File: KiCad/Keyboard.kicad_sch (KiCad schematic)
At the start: 89 parts, among them J1 USB_C_Receptacle, J2 Conn_01x02_Pin, SW1 SW_RESET, SW10 SW_Z, SW11 SW_SUPER, SW12 SW_2, SW13 SW_W, SW14 SW_S, SW15 SW_X, SW16 SW_ALT, SW17 SW_3, SW18 SW_E, SW19 SW_D, SW2 SW_TICK, SW20 SW_C, SW21 SW_SPACE, SW22 SW_4, SW23 SW_R, SW24 SW_F, SW25 SW_V, SW26 SW_5, SW27 SW_T, SW28 SW_G, SW29 SW_6, SW3 SW_TAB, SW4 SW_CAPS, SW5 SW_SHIFT, SW6 SW_CTRL, SW7 SW_1, SW8 SW_Q, SW9 SW_A, U1 ESP32-C6-MINI-1, U2 USBLC6-2SC6, U4 TPS63031DSK, U5 BQ25185DLHR

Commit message: Assign all footprints
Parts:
- C1, C10, C11, C12, C2, C3, C5, C6, C7, C8, C9: footprint (none) -> Capacitor_SMD:C_0603_1608Metric
- D31, D5: footprint (none) -> LED_SMD:LED_0805_2012Metric
- J1: footprint (none) -> Connector_USB:USB_C_Receptacle_JAE_DX07S016JA1R1500
- J2: footprint (none) -> Connector_JST:JST_PH_S2B-PH-SM4-TB_1x02-1MP_P2.00mm_Horizontal
- L1: footprint (none) -> Inductor_SMD:L_Coilcraft_LPS3010
- R1, R10, R2, R3, R4, R5, R6, R7, R8, R9: footprint (none) -> Resistor_SMD:R_0603_1608Metric
- SW1: footprint (none) -> Button_Switch_SMD:SW_SPDT_CK_JS102011SAQN
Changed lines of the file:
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@@
 			)
 		)
-		(property "Footprint" ""
+		(property "Footprint" "Capacitor_SMD:C_0603_1608Metric"
 			(at 243.84 96.52 0)
 			(hide yes)
@@
 			)
 		)
-		(property "Footprint" ""
+		(property "Footprint" "LED_SMD:LED_0805_2012Metric"
 			(at 279.4 77.47 0)
 			(hide yes)
@@
 			)
 		)
-		(property "Footprint" ""
+		(property "Footprint" "LED_SMD:LED_0805_2012Metric"
 			(at 218.44 115.57 0)
 			(hide yes)
@@
 			)
 		)
-		(property "Footprint" ""
+		(property "Footprint" "Resistor_SMD:R_0603_1608Metric"
 			(at 71.12 167.64 0)
 			(hide yes)
@@
 			)
 		)
-		(property "Footprint" ""
+		(property "Footprint" "Resistor_SMD:R_0603_1608Metric"
 			(at 194.31 48.26 0)
 			(hide yes)
@@
 			)
 		)
-		(property "Footprint" ""
+		(property "Footprint" "Capacitor_SMD:C_0603_1608Metric"
 			(at 278.13 127 0)
 			(hide yes)
@@
 			)
 		)
-		(property "Footprint" ""
+		(property "Footprint" "Inductor_SMD:L_Coilcraft_LPS3010"
 			(at 241.3 120.65 0)
 			(hide yes)
@@
 			)
 		)
-		(property "Footprint" ""
+		(property "Footprint" "Resistor_SMD:R_0603_1608Metric"
 			(at 139.7 139.7 0)
 			(hide yes)
@@
 			)
 		)
-		(property "Footprint" ""
+		(property "Footprint" "Resistor_SMD:R_0603_1608Metric"
 			(at 133.35 163.83 0)
 			(hide yes)
@@
 			)
 		)
-		(property "Footprint" ""
+		(property "Footprint" "Resistor_SMD:R_0603_1608Metric"
 			(at 149.86 146.05 0)
 			(hide yes)
@@
 			)
 		)
-		(property "Footprint" ""
+		(property "Footprint" "Capacitor_SMD:C_0603_1608Metric"
 			(at 82.55 132.08 0)
 			(hide yes)
@@
 			)
 		)
-		(property "Footprint" ""
+		(property "Footprint" "Connector_JST:JST_PH_S2B-PH-SM4-TB_1x02-1MP_P2.00mm_Horizontal"
 			(at 156.21 184.15 0)
 			(hide yes)
@@
 			)
 		)
-		(property "Footprint" ""
+		(property "Footprint" "Capacitor_SMD:C_0603_1608Metric"
 			(at 269.24 127 0)
 			(hide yes)
@@
 			)
 		)
-		(property "Footprint" ""
+		(property "Footprint" "Button_Switch_SMD:SW_SPDT_CK_JS102011SAQN"
 			(at 44.45 134.62 0)
 			(hide yes)
@@
 			)
 		)
-		(property "Footprint" ""
+		(property "Footprint" "Capacitor_SMD:C_0603_1608Metric"
 			(at 44.45 146.05 0)
 			(hide yes)
@@
 			)
 		)
-		(property "Footprint" ""
+		(property "Footprint" "Capacitor_SMD:C_0603_1608Metric"
 			(at 167.64 161.29 0)
 			(hide yes)
@@
 			)
 		)
-		(property "Footprint" ""
+		(property "Footprint" "Resistor_SMD:R_0603_1608Metric"
 			(at 267.97 45.72 0)
 			(hide yes)
@@
 			)
 		)
-		(property "Footprint" ""
+		(property "Footprint" "Connector_USB:USB_C_Receptacle_JAE_DX07S016JA1R1500"
 			(at 247.65 29.21 0)
 			(hide yes)
@@
 			)
 		)
-		(property "Footprint" ""
+		(property "Footprint" "Capacitor_SMD:C_0603_1608Metric"
 			(at 157.48 119.38 0)
 			(hide yes)
@@
 			)
 		)
-		(property "Footprint" ""
+		(property "Footprint" "Capacitor_SMD:C_0603_1608Metric"
 			(at 229.87 144.78 0)
 			(hide yes)
@@
 			)
 		)
-		(property "Footprint" ""
+		(property "Footprint" "Resistor_SMD:R_0603_1608Metric"
 			(at 63.5 134.62 0)
 			(hide yes)
@@
 			)
 		)
-		(property "Footprint" ""
+		(property "Footprint" "Resistor_SMD:R_0603_1608Metric"
 			(at 279.4 86.36 0)
 			(hide yes)
@@
 			)
 		)
-		(property "Footprint" ""
+		(property "Footprint" "Capacitor_SMD:C_0603_1608Metric"
 			(at 63.5 146.05 0)
 			(hide yes)
@@
 			)
 		)
-		(property "Footprint" ""
+		(property "Footprint" "Capacitor_SMD:C_0603_1608Metric"
 			(at 146.05 175.26 0)
 			(hide yes)
@@
 			)
 		)
-		(property "Footprint" ""
+		(property "Footprint" "Capacitor_SMD:C_0603_1608Metric"
 			(at 96.52 132.08 0)
 			(hide yes)
@@
 			)
 		)
-		(property "Footprint" ""
+		(property "Footprint" "Resistor_SMD:R_0603_1608Metric"
 			(at 265.43 55.88 0)
 			(hide yes)
@@
 			)
 		)
-		(property "Footprint" ""
+		(property "Footprint" "Resistor_SMD:R_0603_1608Metric"
 			(at 218.44 104.14 0)
 			(hide yes)

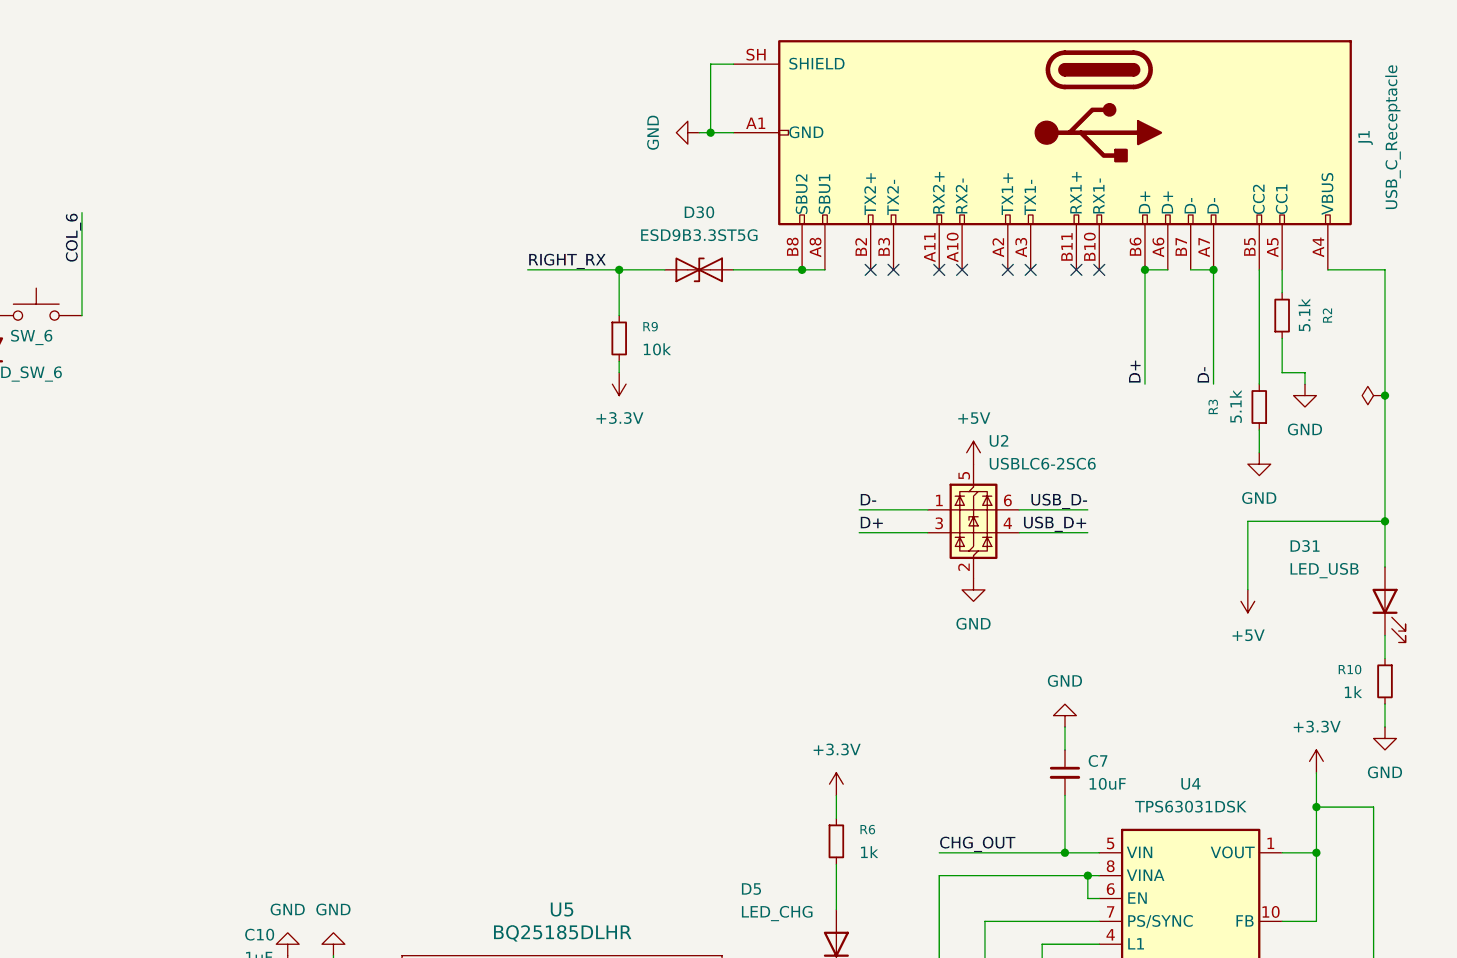
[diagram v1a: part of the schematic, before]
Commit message: Switch to 16-pin USBC
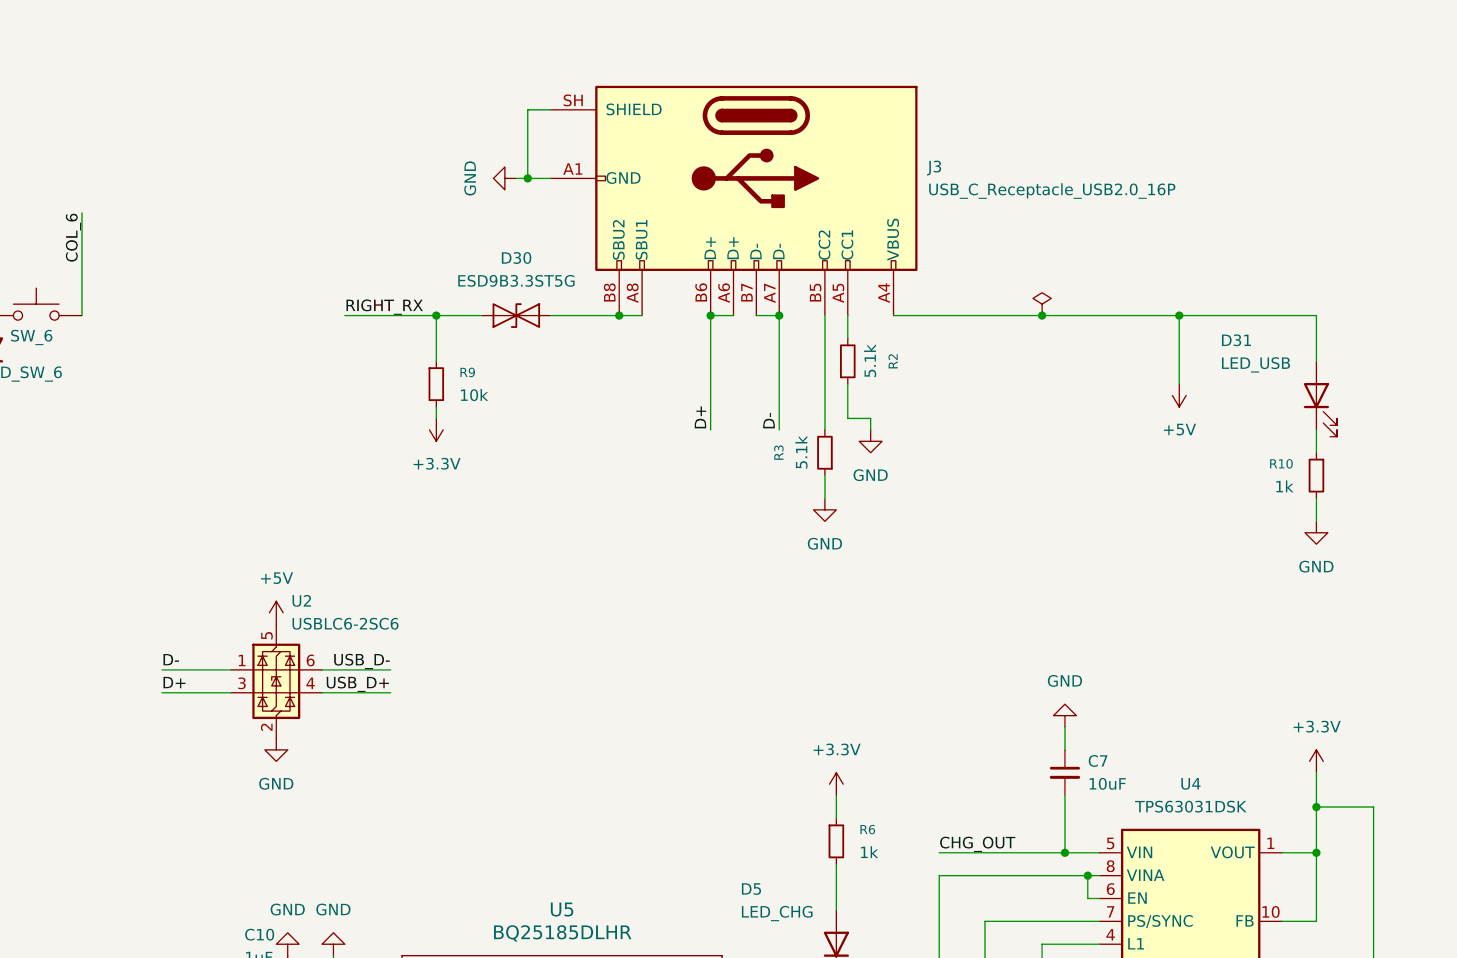
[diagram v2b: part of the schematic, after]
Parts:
- removed J1: USB_C_Receptacle, Connector_USB:USB_C_Receptacle_JAE_DX07S016JA1R1500, symbol Connector:USB_C_Receptacle
- added J3: USB_C_Receptacle_USB2.0_16P, Connector_USB:USB_C_Receptacle_JAE_DX07S016JA1R1500, symbol Connector:USB_C_Receptacle_USB2.0_16P
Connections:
- net +5V: now also J3.A4 (VBUS), J3.A9 (VBUS), J3.B4 (VBUS), J3.B9 (VBUS)
- net D+: now also J3.A6 (D+), J3.B6 (D+)
- net D-: now also J3.A7 (D-), J3.B7 (D-)
- net GND: now also J3.A1 (GND), J3.A12 (GND), J3.B1 (GND), J3.B12 (GND), J3.SH (SHIELD)
- net at D30.2 (A2): now also J3.A8 (SBU1), J3.B8 (SBU2)
- net at R2.2: now also J3.A5 (CC1)
- net at R3.2: now also J3.B5 (CC2)
- no-connect marks 12 -> 4
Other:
- moved on the sheet: D30, D31, R10, R2, R3, R9, U2

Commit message: Start PCB layout
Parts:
- C10, C11, C12: footprint Capacitor_SMD:C_0603_1608Metric -> Capacitor_SMD:C_0402_1005Metric
- R7, R8: footprint Resistor_SMD:R_0603_1608Metric -> Resistor_SMD:R_0402_1005Metric
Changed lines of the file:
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@@
 			)
 		)
-		(property "Footprint" "Resistor_SMD:R_0603_1608Metric"
+		(property "Footprint" "Resistor_SMD:R_0402_1005Metric"
 			(at 139.7 139.7 0)
 			(hide yes)
@@
 			)
 		)
-		(property "Footprint" "Resistor_SMD:R_0603_1608Metric"
+		(property "Footprint" "Resistor_SMD:R_0402_1005Metric"
 			(at 133.35 163.83 0)
 			(hide yes)
@@
 			)
 		)
-		(property "Footprint" "Capacitor_SMD:C_0603_1608Metric"
+		(property "Footprint" "Capacitor_SMD:C_0402_1005Metric"
 			(at 167.64 161.29 0)
 			(hide yes)
@@
 			)
 		)
-		(property "Footprint" "Capacitor_SMD:C_0603_1608Metric"
+		(property "Footprint" "Capacitor_SMD:C_0402_1005Metric"
 			(at 157.48 119.38 0)
 			(hide yes)
@@
 			)
 		)
-		(property "Footprint" "Capacitor_SMD:C_0603_1608Metric"
+		(property "Footprint" "Capacitor_SMD:C_0402_1005Metric"
 			(at 146.05 175.26 0)
 			(hide yes)
